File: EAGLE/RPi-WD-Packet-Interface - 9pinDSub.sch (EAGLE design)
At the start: 21 parts, among them IC1 TLC555, T1 2N3904, T2 2N3904, T3 2N3904

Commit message: Update JP part numbers, new BOM export
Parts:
- renumbered JP6 to JP2
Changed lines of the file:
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@@
 <part name="T3" library="transistor" deviceset="2N3904" device=""/>
 <part name="PE2" library="SparkFun-Aesthetics" deviceset="GND" device=""/>
-<part name="JP6" library="SparkFun-Connectors" deviceset="DB9" device="FEMALE" value="Radio"/>
+<part name="JP2" library="SparkFun-Connectors" deviceset="DB9" device="FEMALE" value="Radio"/>
 <part name="PE8" library="SparkFun-Aesthetics" deviceset="GND" device=""/>
 <part name="R1" library="rcl" deviceset="R-US_" device="0207/7" value="10K"/>
@@
 <instance part="T3" gate="G1" x="114.3" y="35.56" rot="MR0"/>
 <instance part="PE2" gate="1" x="111.76" y="27.94"/>
-<instance part="JP6" gate="G$1" x="139.7" y="55.88"/>
+<instance part="JP2" gate="G$1" x="139.7" y="55.88"/>
 <instance part="PE8" gate="1" x="0" y="45.72"/>
 <instance part="R1" gate="G$1" x="40.64" y="55.88" rot="R270"/>
@@
 </segment>
 <segment>
-<pinref part="JP6" gate="G$1" pin="3"/>
+<pinref part="JP2" gate="G$1" pin="3"/>
 <wire x1="132.08" y1="55.88" x2="127" y2="55.88" width="0.1524" layer="91"/>
 <label x="127" y="55.88" size="1.778" layer="95"/>
@@
 <net name="TXAUDIO" class="0">
 <segment>
-<pinref part="JP6" gate="G$1" pin="1"/>
+<pinref part="JP2" gate="G$1" pin="1"/>
 <wire x1="132.08" y1="60.96" x2="127" y2="60.96" width="0.1524" layer="91"/>
 <label x="121.92" y="60.96" size="1.778" layer="95"/>
@@
 <net name="RXAUDIO" class="0">
 <segment>
-<pinref part="JP6" gate="G$1" pin="5"/>
+<pinref part="JP2" gate="G$1" pin="5"/>
 <wire x1="132.08" y1="50.8" x2="127" y2="50.8" width="0.1524" layer="91"/>
 <label x="121.92" y="50.8" size="1.778" layer="95"/>
@@
 </segment>
 <segment>
-<pinref part="JP6" gate="G$1" pin="6"/>
+<pinref part="JP2" gate="G$1" pin="6"/>
 <wire x1="147.32" y1="58.42" x2="152.4" y2="58.42" width="0.1524" layer="91"/>
 <label x="147.32" y="58.42" size="1.778" layer="95"/>

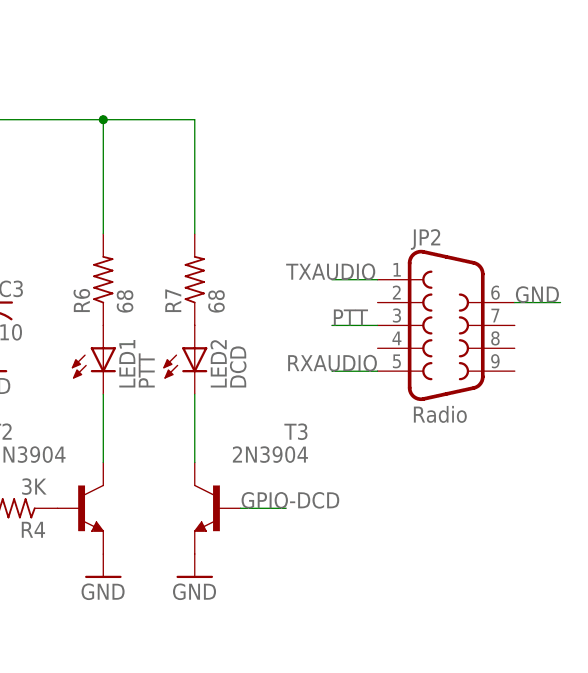
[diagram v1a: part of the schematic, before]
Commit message: Updates after first assembly
Added DCD LED bias resistor, text, widened board for additional mount
hole clearance.
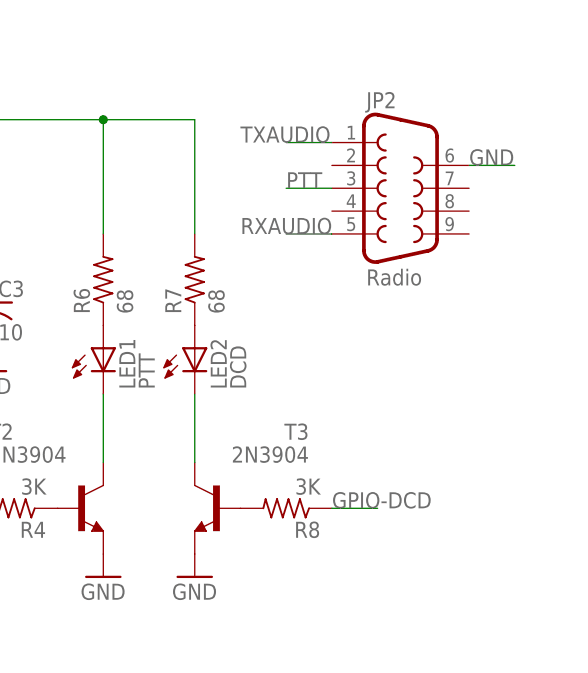
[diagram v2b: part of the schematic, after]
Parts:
- added R8: 3K, rcl:R-US_0207/7
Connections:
- new net N$10: R8.2, T3.B
- net GPIO-DCD: now also R8.1; no longer T3.B
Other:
- moved on the sheet: JP2
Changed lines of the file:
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@@
 <part name="PE8" library="SparkFun-Aesthetics" deviceset="GND" device=""/>
 <part name="R1" library="rcl" deviceset="R-US_" device="0207/7" value="10K"/>
+<part name="R8" library="rcl" deviceset="R-US_" device="0207/7" value="3K"/>
 </parts>
 <sheets>
@@
 <instance part="T3" gate="G1" x="114.3" y="35.56" rot="MR0"/>
 <instance part="PE2" gate="1" x="111.76" y="27.94"/>
-<instance part="JP2" gate="G$1" x="139.7" y="55.88"/>
+<instance part="JP2" gate="G$1" x="134.62" y="71.12"/>
 <instance part="PE8" gate="1" x="0" y="45.72"/>
 <instance part="R1" gate="G$1" x="40.64" y="55.88" rot="R270"/>
+<instance part="R8" gate="G$1" x="121.92" y="35.56" rot="R180"/>
 </instances>
 <busses>
@@
 <segment>
 <pinref part="JP2" gate="G$1" pin="3"/>
-<wire x1="132.08" y1="55.88" x2="127" y2="55.88" width="0.1524" layer="91"/>
-<label x="127" y="55.88" size="1.778" layer="95"/>
+<wire x1="127" y1="71.12" x2="121.92" y2="71.12" width="0.1524" layer="91"/>
+<label x="121.92" y="71.12" size="1.778" layer="95"/>
 </segment>
 </net>
@@
 <segment>
 <pinref part="JP2" gate="G$1" pin="1"/>
-<wire x1="132.08" y1="60.96" x2="127" y2="60.96" width="0.1524" layer="91"/>
-<label x="121.92" y="60.96" size="1.778" layer="95"/>
+<wire x1="127" y1="76.2" x2="121.92" y2="76.2" width="0.1524" layer="91"/>
+<label x="116.84" y="76.2" size="1.778" layer="95"/>
 </segment>
 <segment>
@@
 <segment>
 <pinref part="JP2" gate="G$1" pin="5"/>
-<wire x1="132.08" y1="50.8" x2="127" y2="50.8" width="0.1524" layer="91"/>
-<label x="121.92" y="50.8" size="1.778" layer="95"/>
+<wire x1="127" y1="66.04" x2="121.92" y2="66.04" width="0.1524" layer="91"/>
+<label x="116.84" y="66.04" size="1.778" layer="95"/>
 </segment>
 <segment>
@@
 <segment>
 <pinref part="JP2" gate="G$1" pin="6"/>
-<wire x1="147.32" y1="58.42" x2="152.4" y2="58.42" width="0.1524" layer="91"/>
-<label x="147.32" y="58.42" size="1.778" layer="95"/>
+<wire x1="142.24" y1="73.66" x2="147.32" y2="73.66" width="0.1524" layer="91"/>
+<label x="142.24" y="73.66" size="1.778" layer="95"/>
 </segment>
 <segment>
@@
 </segment>
 <segment>
-<pinref part="T3" gate="G1" pin="B"/>
-<wire x1="116.84" y1="35.56" x2="121.92" y2="35.56" width="0.1524" layer="91"/>
-<label x="116.84" y="35.56" size="1.778" layer="95"/>
+<pinref part="R8" gate="G$1" pin="1"/>
+<wire x1="127" y1="35.56" x2="132.08" y2="35.56" width="0.1524" layer="91"/>
+<label x="127" y="35.56" size="1.778" layer="95"/>
 </segment>
 </net>
@@
 </segment>
 </net>
+<net name="N$10" class="0">
+<segment>
+<pinref part="T3" gate="G1" pin="B"/>
+<pinref part="R8" gate="G$1" pin="2"/>
+</segment>
+</net>

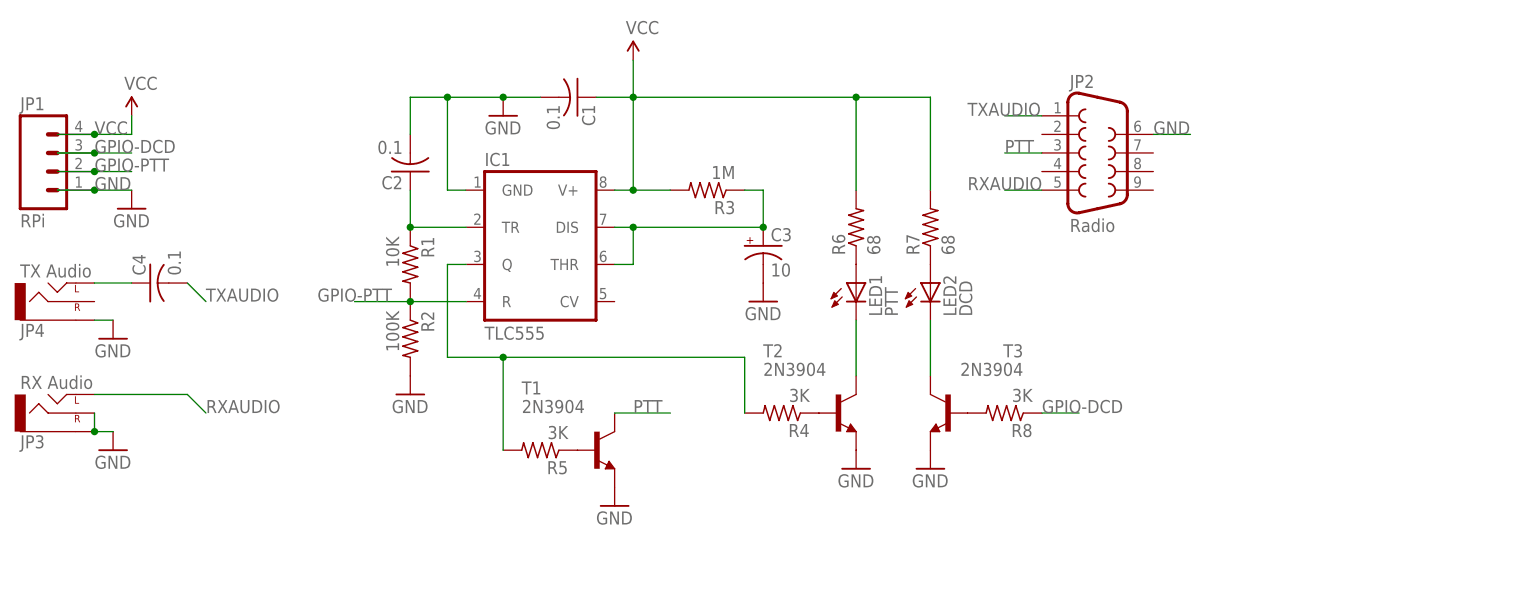
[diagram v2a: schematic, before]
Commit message: Design update to v1.1
Added channel selection jumpers for RX/TX, single-line PTT resistor
jumper, TX audio level pot, timeout delay pot (0-2 mins /w specified
values). Moved to Dangerous Prototypes 'Sick of Beige' 60mm x 60mm PCB
layout standard.
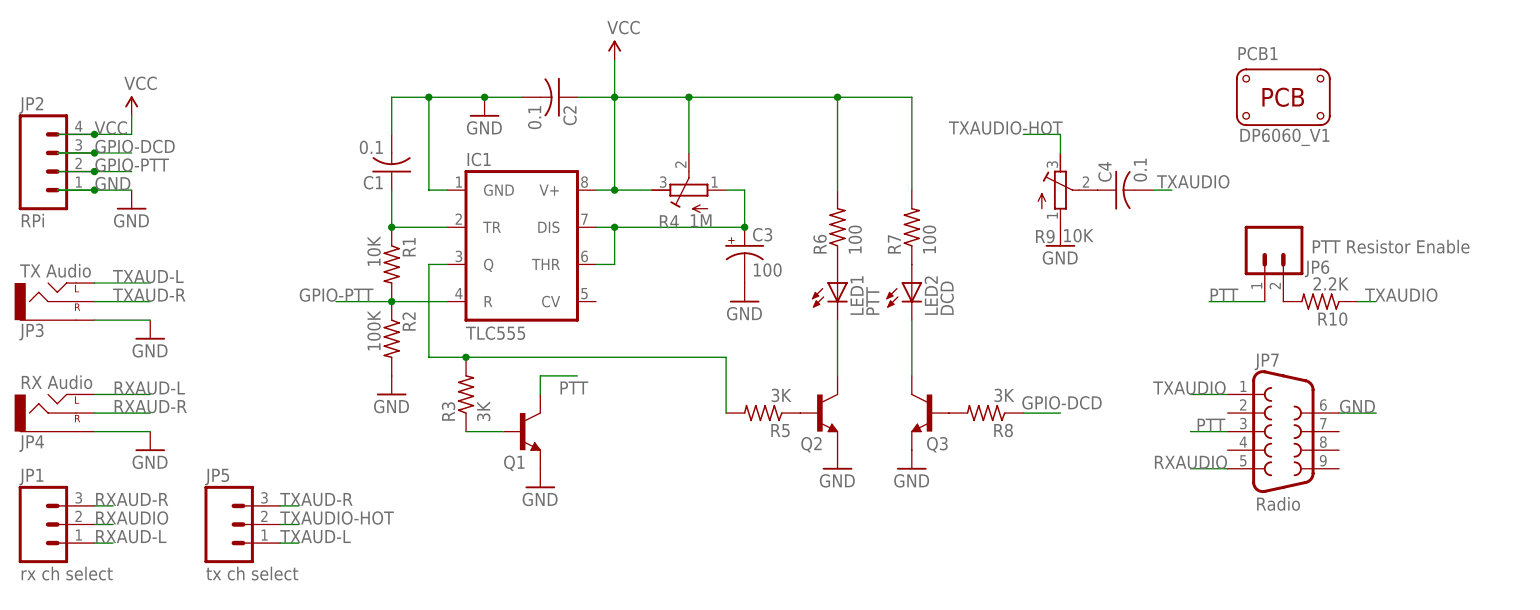
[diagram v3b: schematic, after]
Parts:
- removed T1, T2, T3: 2N3904, transistor:2N3904
- added JP5: tx ch select, SparkFun-Connectors:M03PTH
- added JP6: PTT Resistor Enable, SparkFun-Connectors:M02PTH
- added JP7: Radio, SparkFun-Connectors:DB9FEMALE
- added PCB1: PCB_DP_SQUARE-6X6, dp_devices:PCB_DP_SQUARE-6X6
- added Q1: PTT, SparkFun-DiscreteSemi:TRANSISTOR_NPNTO-92-AMMO
- added Q2: PTT-LED, SparkFun-DiscreteSemi:TRANSISTOR_NPNTO-92-AMMO
- added Q3: DCD-LED, SparkFun-DiscreteSemi:TRANSISTOR_NPNTO-92-AMMO
- added R10: 2.2K, rcl:R-US_0207/7
- added R9: 10K, GeekAmmo:RTRIM-3362P
- C3: value 10 -> 100
- JP1: value RPi -> rx ch select; device SparkFun-Connectors:M04PTH -> SparkFun-Connectors:M03PTH
- JP2: value Radio -> RPi; device SparkFun-Connectors:DB9FEMALE -> SparkFun-Connectors:M04PTH
- JP3: value RX Audio -> TX Audio
- JP4: value TX Audio -> RX Audio
- R3: value 1M -> 3K
- R4: value 3K -> 1M; device rcl:R-US_0207/7 -> rcl:R-TRIMM3296W
- R6, R7: value 68 -> 100
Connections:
- new net N$11: JP6.2, R10.2
- new net RXAUD-L: JP1.1, JP4.LEFT
- new net RXAUD-R: JP1.3, JP4.RIGHT
- new net TXAUD-L: JP3.LEFT, JP5.1
- new net TXAUD-R: JP3.RIGHT, JP5.3
- new net TXAUDIO-HOT: JP5.2, R9.3
- net GND: now also JP2.1, JP7.6, Q1.E, Q2.E, Q3.E, R9.1; no longer JP1.1, JP2.6, JP3.RIGHT, T1.E, T2.E, T3.E
- net GPIO-DCD: now also JP2.3; no longer JP1.3
- net GPIO-PTT: now also JP2.2; no longer JP1.2
- net N$10: now also Q3.B; no longer T3.B
- net N$3: now also C1.1; no longer C2.1
- net N$4: now also R9.2; no longer JP4.LEFT
- net N$5: now also R4.A; no longer R3.1
- net N$6: now also Q2.C; no longer T2.C
- net N$7: now also Q2.B, R5.1; no longer R4.1, T2.B
- net N$8: now also Q1.B, R3.1; no longer R5.1, T1.B
- net N$9: now also Q3.C; no longer T3.C
- net PTT: now also JP6.1, JP7.3, Q1.C; no longer JP2.3, T1.C
- net PTT_TRIGGER: now also R3.2; no longer R4.2
- net RXAUDIO: now also JP1.2, JP7.5; no longer JP2.5, JP3.LEFT
- net TXAUDIO: now also JP7.1, R10.1; no longer JP2.1
- net VCC: now also C2.1, JP2.4, R4.E, R4.S; no longer C1.1, JP1.4, R3.2
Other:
- moved on the sheet: C1, C2, C3, C4, IC1, JP3, JP4, LED1, LED2, R1, R2, R3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

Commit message: Update PCB to v1.1a, add images of board and schematic
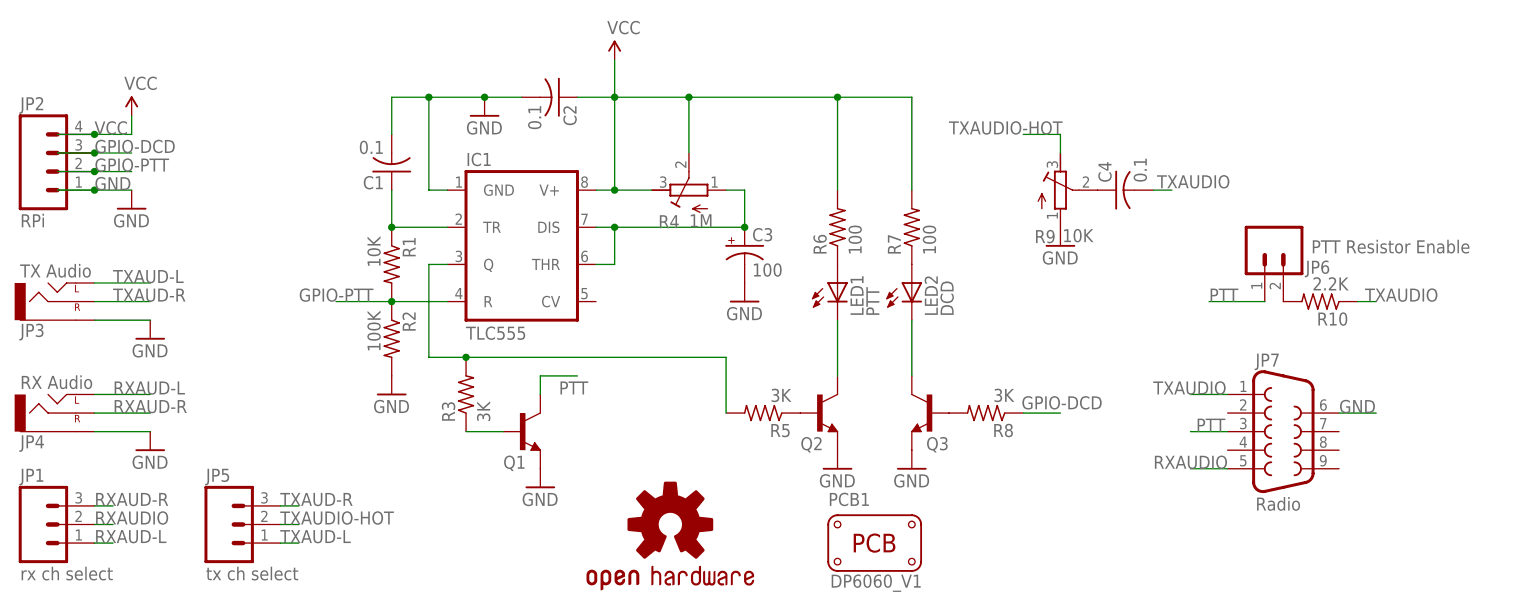
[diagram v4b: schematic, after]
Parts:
- added LOGO1: OSHW-LOGOM, SparkFun-Aesthetics:OSHW-LOGOM
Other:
- moved on the sheet: PCB1
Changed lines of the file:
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@@
 <grid distance="0.1" unitdist="inch" unit="inch" style="lines" multiple="1" display="no" altdistance="0.01" altunitdist="inch" altunit="inch"/>
 <layers>
-<layer number="1" name="Top" color="4" fill="1" visible="no" active="no"/>
-<layer number="16" name="Bottom" color="1" fill="1" visible="no" active="no"/>
-<layer number="17" name="Pads" color="2" fill="1" visible="no" active="no"/>
-<layer number="18" name="Vias" color="2" fill="1" visible="no" active="no"/>
-<layer number="19" name="Unrouted" color="6" fill="1" visible="no" active="no"/>
-<layer number="20" name="Dimension" color="15" fill="1" visible="no" active="no"/>
-<layer number="21" name="tPlace" color="15" fill="1" visible="no" active="no"/>
-<layer number="22" name="bPlace" color="7" fill="1" visible="no" active="no"/>
-<layer number="23" name="tOrigins" color="15" fill="1" visible="no" active="no"/>
-<layer number="24" name="bOrigins" color="15" fill="1" visible="no" active="no"/>
-<layer number="25" name="tNames" color="7" fill="1" visible="no" active="no"/>
-<layer number="26" name="bNames" color="7" fill="1" visible="no" active="no"/>
-<layer number="27" name="tValues" color="7" fill="1" visible="no" active="no"/>
-<layer number="28" name="bValues" color="7" fill="1" visible="no" active="no"/>
+<layer number="1" name="Top" color="4" fill="1" visible="yes" active="no"/>
+<layer number="16" name="Bottom" color="1" fill="1" visible="yes" active="no"/>
+<layer number="17" name="Pads" color="2" fill="1" visible="yes" active="no"/>
+<layer number="18" name="Vias" color="2" fill="1" visible="yes" active="no"/>
+<layer number="19" name="Unrouted" color="6" fill="1" visible="yes" active="no"/>
+<layer number="20" name="Dimension" color="15" fill="1" visible="yes" active="no"/>
+<layer number="21" name="tPlace" color="15" fill="1" visible="yes" active="no"/>
+<layer number="22" name="bPlace" color="7" fill="1" visible="yes" active="no"/>
+<layer number="23" name="tOrigins" color="15" fill="1" visible="yes" active="no"/>
+<layer number="24" name="bOrigins" color="15" fill="1" visible="yes" active="no"/>
+<layer number="25" name="tNames" color="7" fill="1" visible="yes" active="no"/>
+<layer number="26" name="bNames" color="7" fill="1" visible="yes" active="no"/>
+<layer number="27" name="tValues" color="7" fill="1" visible="yes" active="no"/>
+<layer number="28" name="bValues" color="7" fill="1" visible="yes" active="no"/>
 <layer number="29" name="tStop" color="7" fill="3" visible="no" active="no"/>
 <layer number="30" name="bStop" color="7" fill="6" visible="no" active="no"/>
@@
 <layer number="35" name="tGlue" color="7" fill="4" visible="no" active="no"/>
 <layer number="36" name="bGlue" color="7" fill="5" visible="no" active="no"/>
-<layer number="37" name="tTest" color="7" fill="1" visible="no" active="no"/>
-<layer number="38" name="bTest" color="7" fill="1" visible="no" active="no"/>
+<layer number="37" name="tTest" color="7" fill="1" visible="yes" active="no"/>
+<layer number="38" name="bTest" color="7" fill="1" visible="yes" active="no"/>
 <layer number="39" name="tKeepout" color="4" fill="11" visible="no" active="no"/>
 <layer number="40" name="bKeepout" color="1" fill="11" visible="no" active="no"/>
@@
 <layer number="44" name="Drills" color="7" fill="1" visible="no" active="no"/>
 <layer number="45" name="Holes" color="7" fill="1" visible="no" active="no"/>
-<layer number="46" name="Milling" color="3" fill="1" visible="no" active="no"/>
-<layer number="47" name="Measures" color="7" fill="1" visible="no" active="no"/>
-<layer number="48" name="Document" color="7" fill="1" visible="no" active="no"/>
-<layer number="49" name="Reference" color="7" fill="1" visible="no" active="no"/>
-<layer number="50" name="dxf" color="7" fill="1" visible="no" active="no"/>
-<layer number="51" name="tDocu" color="7" fill="1" visible="no" active="no"/>
-<layer number="52" name="bDocu" color="7" fill="1" visible="no" active="no"/>
-<layer number="53" name="tGND_GNDA" color="7" fill="9" visible="no" active="no"/>
-<layer number="54" name="bGND_GNDA" color="1" fill="9" visible="no" active="no"/>
-<layer number="56" name="wert" color="7" fill="1" visible="no" active="no"/>
-<layer number="57" name="tCAD" color="7" fill="1" visible="no" active="no"/>
-<layer number="59" name="tCarbon" color="7" fill="1" visible="no" active="no"/>
-<layer number="60" name="bCarbon" color="7" fill="1" visible="no" active="no"/>
+<layer number="46" name="Milling" color="3" fill="1" visible="yes" active="no"/>
+<layer number="47" name="Measures" color="7" fill="1" visible="yes" active="no"/>
+<layer number="48" name="Document" color="7" fill="1" visible="yes" active="no"/>
+<layer number="49" name="Reference" color="7" fill="1" visible="yes" active="no"/>
+<layer number="50" name="dxf" color="7" fill="1" visible="yes" active="no"/>
+<layer number="51" name="tDocu" color="7" fill="1" visible="yes" active="no"/>
+<layer number="52" name="bDocu" color="7" fill="1" visible="yes" active="no"/>
+<layer number="53" name="tGND_GNDA" color="7" fill="9" visible="yes" active="no"/>
+<layer number="54" name="bGND_GNDA" color="1" fill="9" visible="yes" active="no"/>
+<layer number="56" name="wert" color="7" fill="1" visible="yes" active="no"/>
+<layer number="57" name="tCAD" color="7" fill="1" visible="yes" active="no"/>
+<layer number="59" name="tCarbon" color="7" fill="1" visible="yes" active="no"/>
+<layer number="60" name="bCarbon" color="7" fill="1" visible="yes" active="no"/>
 <layer number="90" name="Modules" color="5" fill="1" visible="yes" active="yes"/>
 <layer number="91" name="Nets" color="2" fill="1" visible="yes" active="yes"/>
@@
 <part name="GND10" library="SparkFun-Aesthetics" deviceset="GND" device=""/>
 <part name="PCB1" library="dp_devices" deviceset="PCB_DP_SQUARE" device="-6X6" value="PCB_DP_SQUARE-6X6"/>
+<part name="LOGO1" library="SparkFun-Aesthetics" deviceset="OSHW-LOGO" device="M"/>
 </parts>
 <sheets>
@@
 </instance>
 <instance part="GND10" gate="1" x="129.54" y="58.42"/>
-<instance part="PCB1" gate="PCB" x="160.02" y="78.74"/>
+<instance part="PCB1" gate="PCB" x="104.14" y="17.78"/>
+<instance part="LOGO1" gate="G$1" x="76.2" y="20.32"/>
 </instances>
 <busses>
